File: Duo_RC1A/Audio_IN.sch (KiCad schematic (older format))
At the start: 126 parts, among them J1 JACK_P10_TRS_6P, J2 JACK_P10_TRS_6P

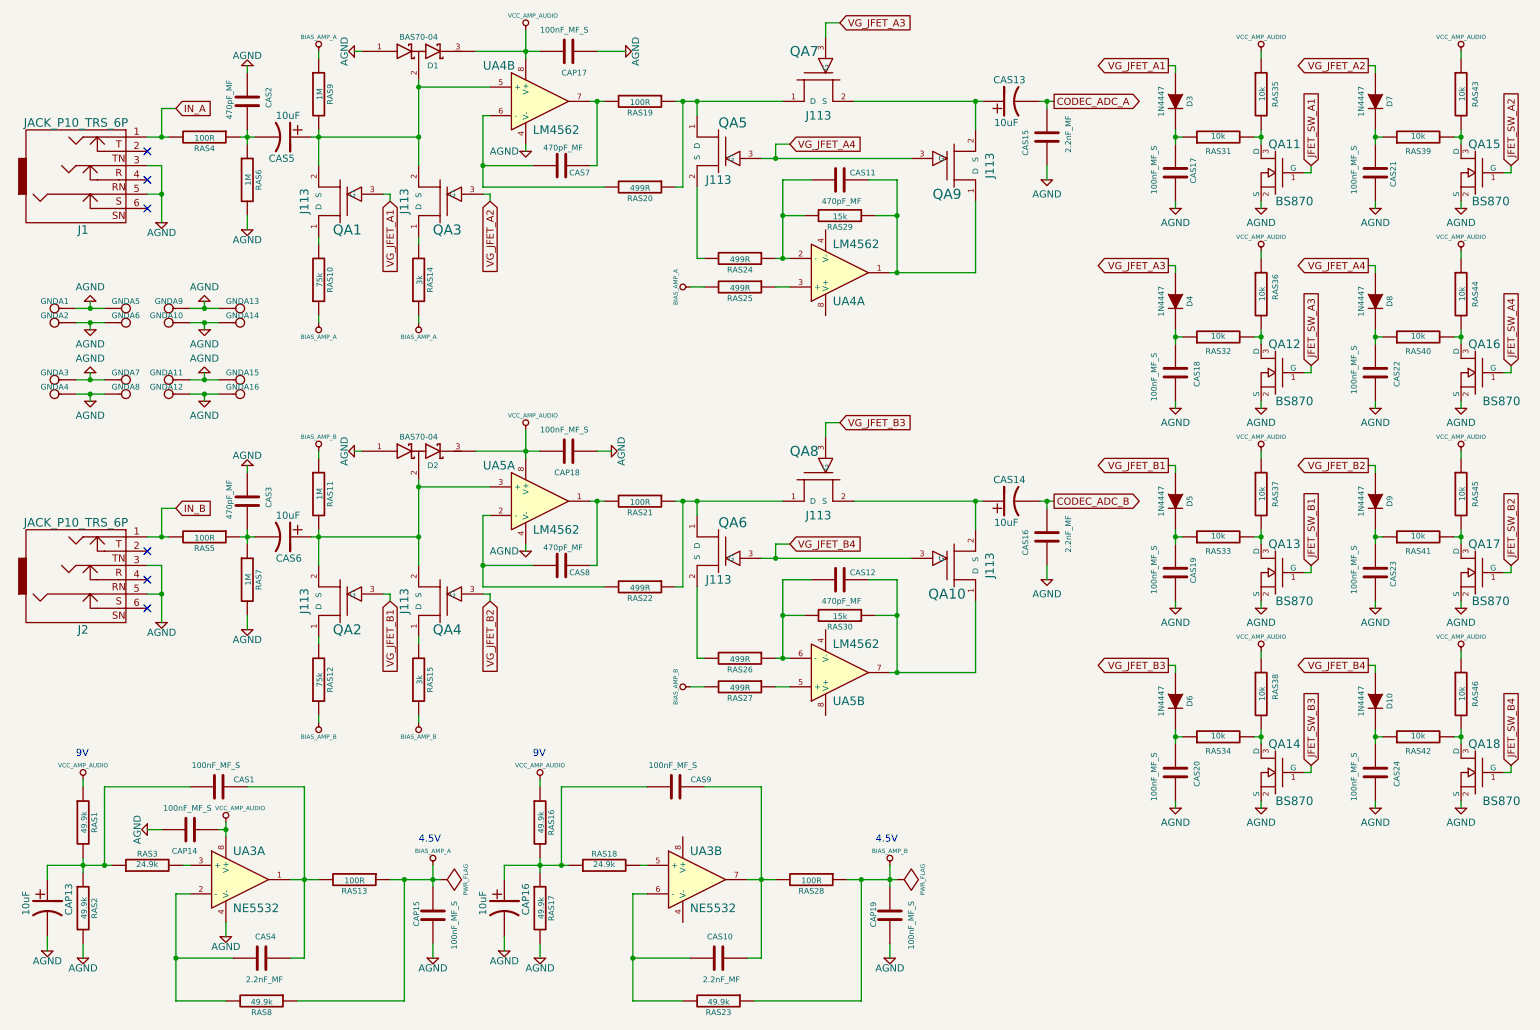
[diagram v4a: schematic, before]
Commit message: Changed the mecanical dimensions. Increase the board outline dimensions and the space of the P10 jacks. Removed the capacitor from the audio switch control circuit.
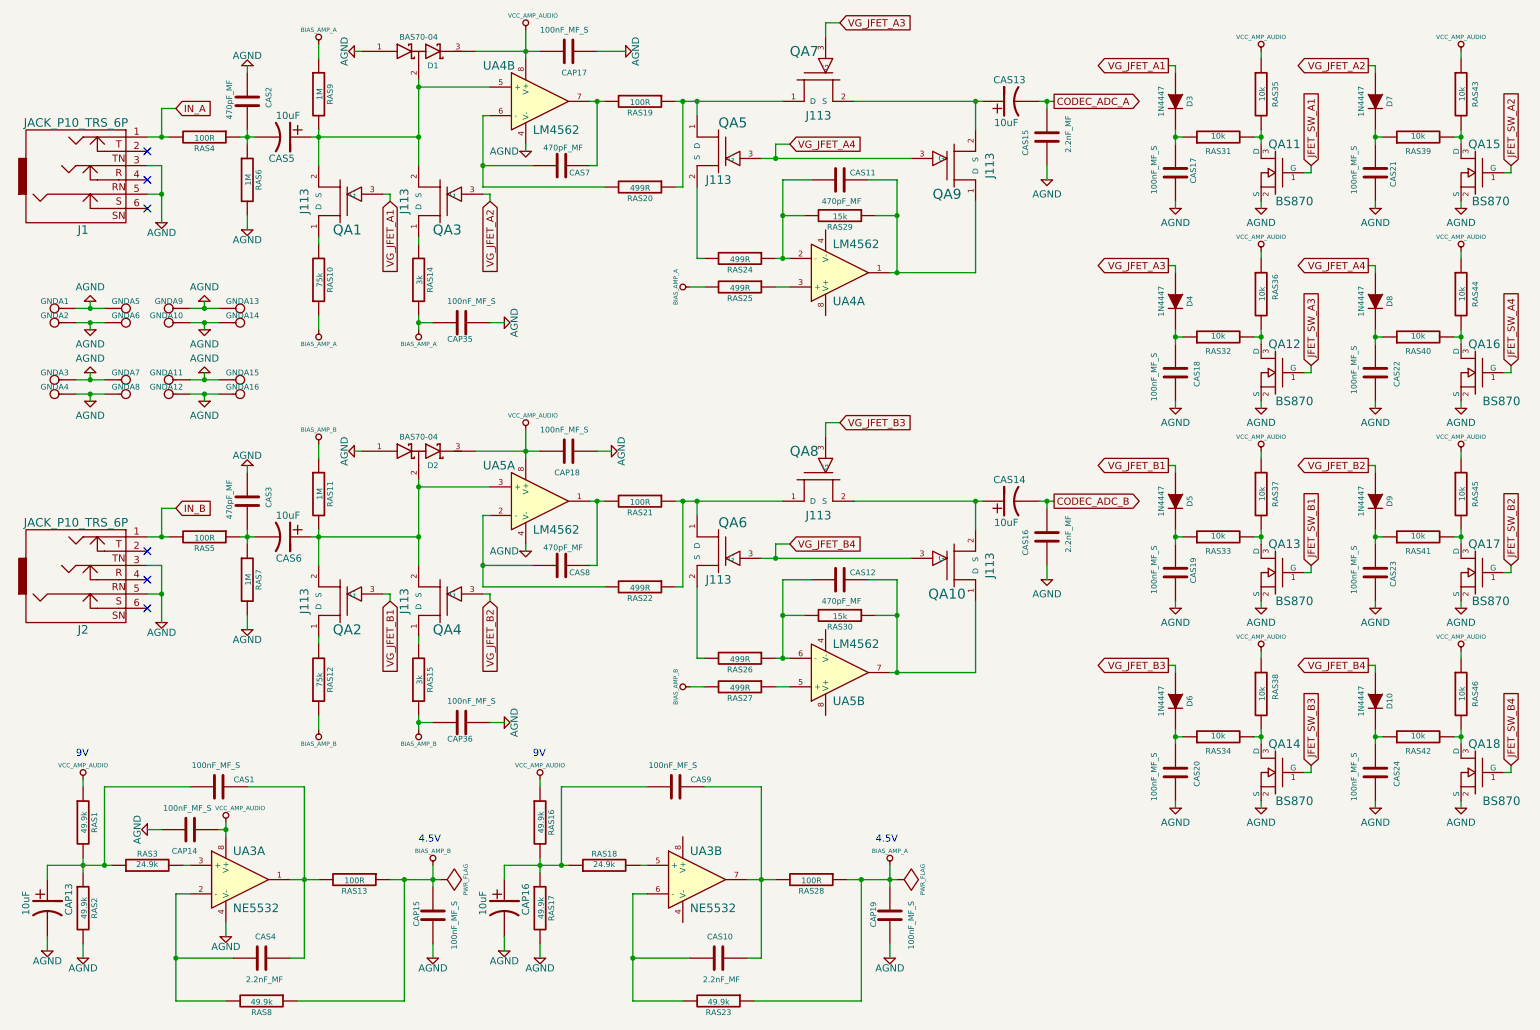
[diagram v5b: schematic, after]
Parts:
- added CAP35, CAP36: 100nF_MF_S, Duo_Audio_HMI_RC1A:CapacitorMetalFilm_7.2x2.5MM_P5MM, symbol C
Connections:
- net AGND: now also CAP35.1, CAP36.1
- net BIAS_AMP_A: now also CAP19.2, RAS23.1, RAS28.1, CAP35.2; no longer CAP15.2, RAS13.1, RAS8.1
- net BIAS_AMP_B: now also CAP15.2, RAS13.1, RAS8.1, CAP36.2; no longer CAP19.2, RAS23.1, RAS28.1
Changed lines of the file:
@@
 L BIAS_AMP_A #PWR0152
 U 1 1 536EB9C8
-P 2650 800
-F 0 "#PWR0152" H 2650 900 30  0001 C CNN
-F 1 "BIAS_AMP_A" H 2650 900 30  0000 C CNN
-F 2 "~" H 2650 800 60  0000 C CNN
-F 3 "~" H 2650 800 60  0000 C CNN
-	1    2650 800
+P 2650 750
+F 0 "#PWR0152" H 2650 850 30  0001 C CNN
+F 1 "BIAS_AMP_A" H 2650 850 30  0000 C CNN
+F 2 "~" H 2650 750 60  0000 C CNN
+F 3 "~" H 2650 750 60  0000 C CNN
+	1    2650 750
 	1    0    0    -1
 $EndComp
@@
 L BIAS_AMP_A #PWR0153
 U 1 1 536EB9D5
-P 2650 2700
-F 0 "#PWR0153" H 2650 2800 30  0001 C CNN
-F 1 "BIAS_AMP_A" H 2650 2800 30  0000 C CNN
-F 2 "~" H 2650 2700 60  0000 C CNN
-F 3 "~" H 2650 2700 60  0000 C CNN
-	1    2650 2700
+P 2650 2750
+F 0 "#PWR0153" H 2650 2850 30  0001 C CNN
+F 1 "BIAS_AMP_A" H 2650 2850 30  0000 C CNN
+F 2 "~" H 2650 2750 60  0000 C CNN
+F 3 "~" H 2650 2750 60  0000 C CNN
+	1    2650 2750
 	-1   0    0    1
 $EndComp
@@
 L BIAS_AMP_A #PWR0154
 U 1 1 536EB9DB
-P 3350 2700
-F 0 "#PWR0154" H 3350 2800 30  0001 C CNN
-F 1 "BIAS_AMP_A" H 3350 2800 30  0000 C CNN
-F 2 "~" H 3350 2700 60  0000 C CNN
-F 3 "~" H 3350 2700 60  0000 C CNN
-	1    3350 2700
+P 3350 2750
+F 0 "#PWR0154" H 3350 2850 30  0001 C CNN
+F 1 "BIAS_AMP_A" H 3350 2850 30  0000 C CNN
+F 2 "~" H 3350 2750 60  0000 C CNN
+F 3 "~" H 3350 2750 60  0000 C CNN
+	1    3350 2750
 	-1   0    0    1
 $EndComp
@@
 L BIAS_AMP_A #PWR0156
 U 1 1 536EC818
-P 3450 6500
-F 0 "#PWR0156" H 3450 6600 30  0001 C CNN
-F 1 "BIAS_AMP_A" H 3450 6600 30  0000 C CNN
-F 2 "~" H 3450 6500 60  0000 C CNN
-F 3 "~" H 3450 6500 60  0000 C CNN
-	1    3450 6500
+P 6650 6500
+F 0 "#PWR0156" H 6650 6600 30  0001 C CNN
+F 1 "BIAS_AMP_A" H 6650 6600 30  0000 C CNN
+F 2 "~" H 6650 6500 60  0000 C CNN
+F 3 "~" H 6650 6500 60  0000 C CNN
+	1    6650 6500
 	1    0    0    -1
 $EndComp
@@
 L BIAS_AMP_B #PWR0157
 U 1 1 536EE5B8
-P 2650 3600
-F 0 "#PWR0157" H 2650 3700 30  0001 C CNN
-F 1 "BIAS_AMP_B" H 2650 3700 30  0000 C CNN
-F 2 "~" H 2650 3600 60  0000 C CNN
-F 3 "~" H 2650 3600 60  0000 C CNN
-	1    2650 3600
+P 2650 3550
+F 0 "#PWR0157" H 2650 3650 30  0001 C CNN
+F 1 "BIAS_AMP_B" H 2650 3650 30  0000 C CNN
+F 2 "~" H 2650 3550 60  0000 C CNN
+F 3 "~" H 2650 3550 60  0000 C CNN
+	1    2650 3550
 	1    0    0    -1
 $EndComp
@@
 L BIAS_AMP_B #PWR0158
 U 1 1 536EE5C5
-P 2650 5500
-F 0 "#PWR0158" H 2650 5600 30  0001 C CNN
-F 1 "BIAS_AMP_B" H 2650 5600 30  0000 C CNN
-F 2 "~" H 2650 5500 60  0000 C CNN
-F 3 "~" H 2650 5500 60  0000 C CNN
-	1    2650 5500
+P 2650 5550
+F 0 "#PWR0158" H 2650 5650 30  0001 C CNN
+F 1 "BIAS_AMP_B" H 2650 5650 30  0000 C CNN
+F 2 "~" H 2650 5550 60  0000 C CNN
+F 3 "~" H 2650 5550 60  0000 C CNN
+	1    2650 5550
 	-1   0    0    1
 $EndComp
@@
 L BIAS_AMP_B #PWR0159
 U 1 1 536EE5CB
-P 3350 5500
-F 0 "#PWR0159" H 3350 5600 30  0001 C CNN
-F 1 "BIAS_AMP_B" H 3350 5600 30  0000 C CNN
-F 2 "~" H 3350 5500 60  0000 C CNN
-F 3 "~" H 3350 5500 60  0000 C CNN
-	1    3350 5500
+P 3350 5550
+F 0 "#PWR0159" H 3350 5650 30  0001 C CNN
+F 1 "BIAS_AMP_B" H 3350 5650 30  0000 C CNN
+F 2 "~" H 3350 5550 60  0000 C CNN
+F 3 "~" H 3350 5550 60  0000 C CNN
+	1    3350 5550
 	-1   0    0    1
 $EndComp
@@
 L BIAS_AMP_B #PWR0161
 U 1 1 536EEA92
-P 6650 6500
-F 0 "#PWR0161" H 6650 6600 30  0001 C CNN
-F 1 "BIAS_AMP_B" H 6650 6600 30  0000 C CNN
-F 2 "~" H 6650 6500 60  0000 C CNN
-F 3 "~" H 6650 6500 60  0000 C CNN
-	1    6650 6500
+P 3450 6500
+F 0 "#PWR0161" H 3450 6600 30  0001 C CNN
+F 1 "BIAS_AMP_B" H 3450 6600 30  0000 C CNN
+F 2 "~" H 3450 6500 60  0000 C CNN
+F 3 "~" H 3450 6500 60  0000 C CNN
+	1    3450 6500
 	1    0    0    -1
 $EndComp
@@
 	2650 1350 2650 1600
 Wire Wire Line
-	2650 800  2650 850
+	2650 750  2650 850
 Connection ~ 2650 1400
 Wire Wire Line
-	2650 2700 2650 2650
-Wire Wire Line
-	3350 2700 3350 2650
+	2650 2750 2650 2650
+Wire Wire Line
+	3350 2750 3350 2650
 Wire Wire Line
 	3800 1250 3850 1250
@@
 	2650 4150 2650 4400
 Wire Wire Line
-	2650 3600 2650 3650
+	2650 3550 2650 3650
 Connection ~ 2650 4200
 Wire Wire Line
-	2650 5500 2650 5450
-Wire Wire Line
-	3350 5500 3350 5450
+	2650 5550 2650 5450
+Wire Wire Line
+	3350 5550 3350 5450
 Wire Wire Line
 	3800 4050 3850 4050
@@
 	5750 1550 6800 1550
 Connection ~ 5850 4350
+$Comp
+L C CAP36
+U 1 1 53861A7E
+P 3650 5500
+F 0 "CAP36" V 3765 5400 40  0000 L CNN
+F 1 "100nF_MF_S" V 3500 5400 40  0000 L CNN
+F 2 "Duo_Audio_HMI_RC1A:CapacitorMetalFilm_7.2x2.5MM_P5MM" H 3688 5350 30  0001 C CNN
+F 3 "~" H 3650 5500 60  0000 C CNN
+	1    3650 5500
+	0    1    1    0
+$EndComp
+$Comp
+L C CAP35
+U 1 1 53861ADE
+P 3650 2700
+F 0 "CAP35" V 3765 2600 40  0000 L CNN
+F 1 "100nF_MF_S" V 3500 2600 40  0000 L CNN
+F 2 "Duo_Audio_HMI_RC1A:CapacitorMetalFilm_7.2x2.5MM_P5MM" H 3688 2550 30  0001 C CNN
+F 3 "~" H 3650 2700 60  0000 C CNN
+	1    3650 2700
+	0    1    1    0
+$EndComp
+Wire Wire Line
+	3350 2700 3450 2700
+Connection ~ 3350 2700
+Wire Wire Line
+	3450 5500 3350 5500
+Connection ~ 3350 5500
+$Comp
+L AGND #PWR0164
+U 1 1 53861E00
+P 3950 5500
+F 0 "#PWR0164" H 3950 5500 40  0001 C CNN
+F 1 "AGND" H 3950 5430 50  0000 C CNN
+F 2 "~" H 3950 5500 60  0000 C CNN
+F 3 "~" H 3950 5500 60  0000 C CNN
+	1    3950 5500
+	0    -1   -1   0
+$EndComp
+Wire Wire Line
+	3850 5500 3950 5500
+$Comp
+L AGND #PWR0165
+U 1 1 538620D0
+P 3950 2700
+F 0 "#PWR0165" H 3950 2700 40  0001 C CNN
+F 1 "AGND" H 3950 2630 50  0000 C CNN
+F 2 "~" H 3950 2700 60  0000 C CNN
+F 3 "~" H 3950 2700 60  0000 C CNN
+	1    3950 2700
+	0    -1   -1   0
+$EndComp
+Wire Wire Line
+	3850 2700 3950 2700
 $EndSCHEMATC

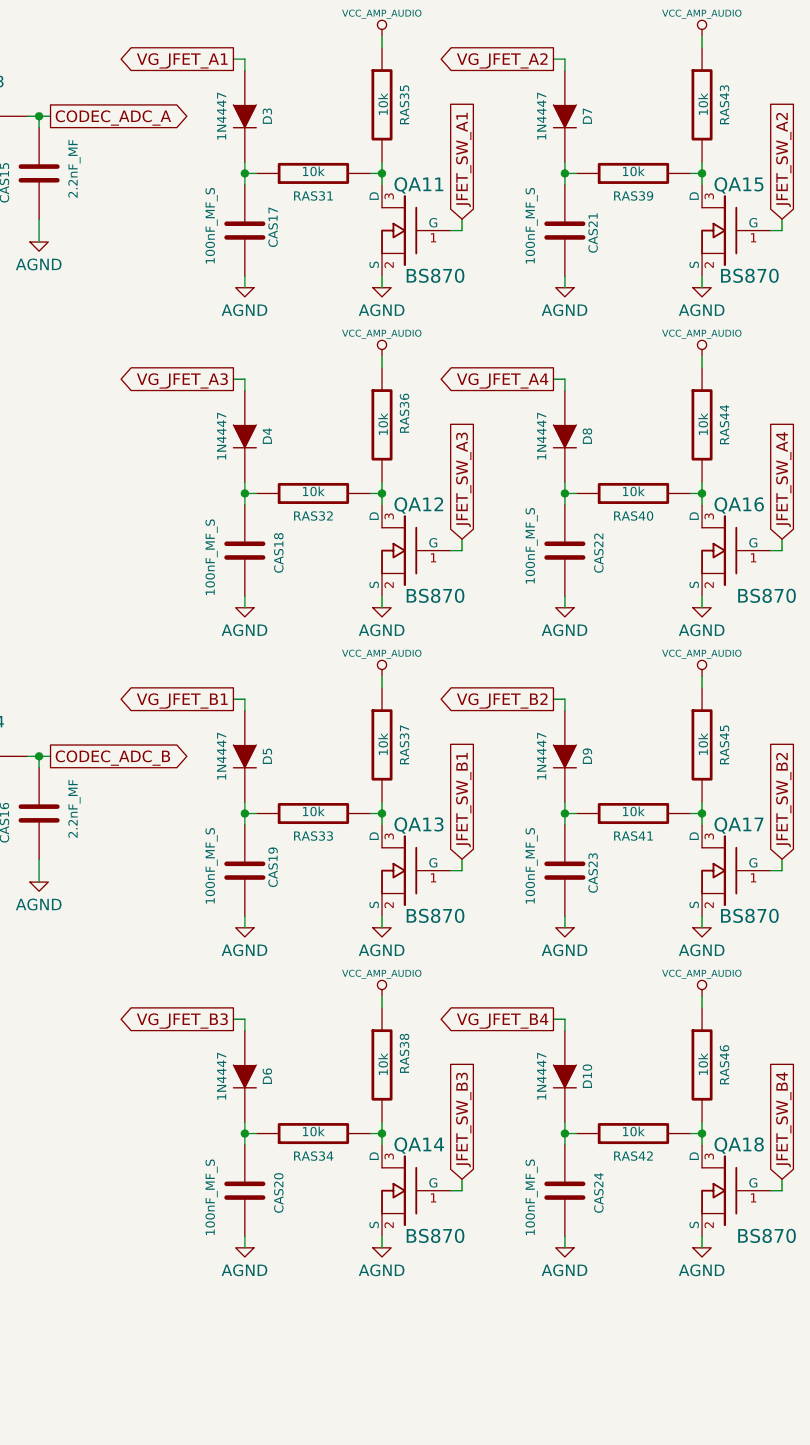
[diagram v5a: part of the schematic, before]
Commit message: Removed CODEC_MITEC signal. Defined the connector between the TopBoard and the BottomBoard. Saved layouts in *.brd old format.
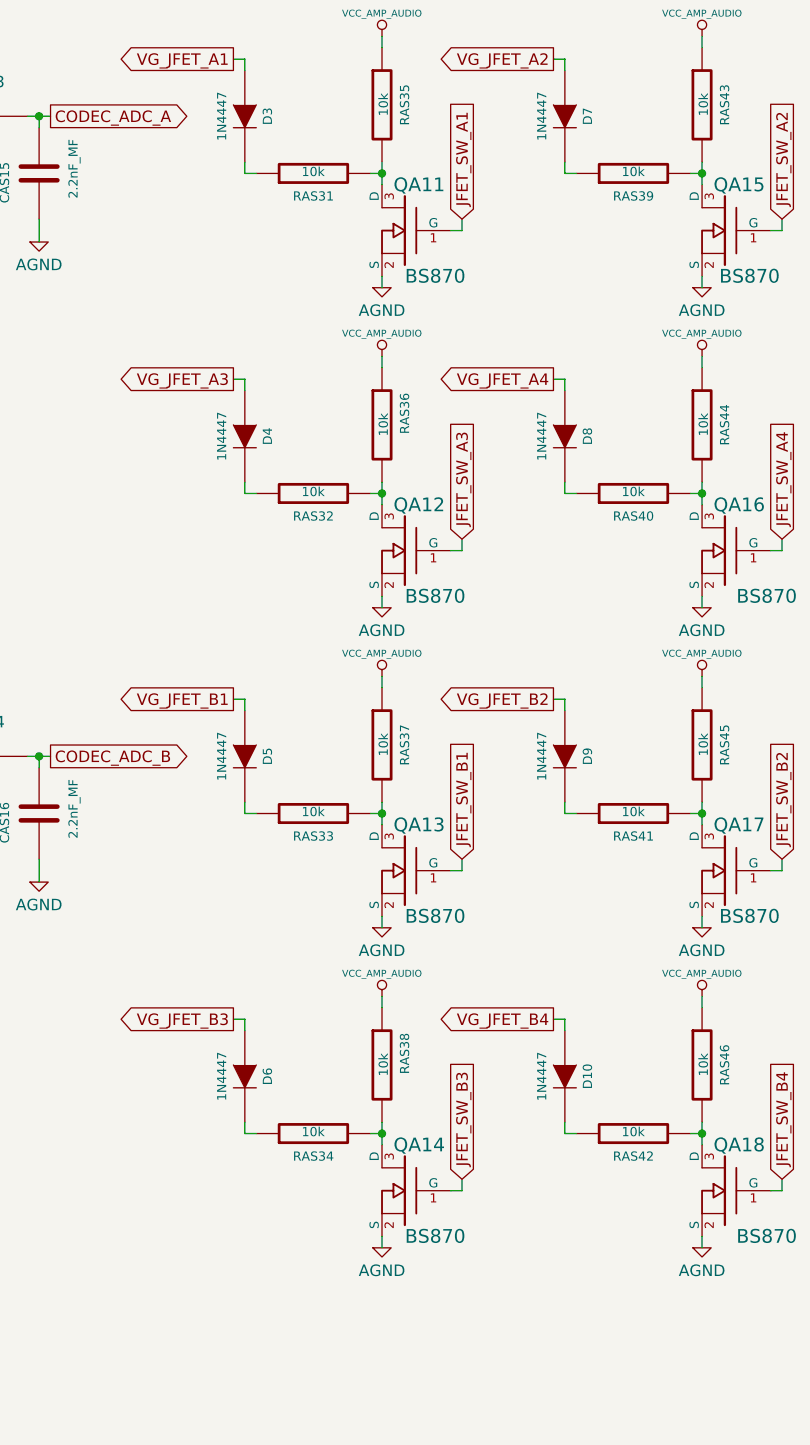
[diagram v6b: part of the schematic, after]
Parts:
- removed CAS17, CAS18, CAS19, CAS20, CAS21, CAS22, CAS23, CAS24: 100nF_MF_S, Duo_Audio_HMI_RC1A:CapacitorMetalFilm_7.2x2.5MM_P5MM, symbol C
